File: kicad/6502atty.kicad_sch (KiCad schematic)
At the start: 27 parts, among them J10 Conn_01x04_Pin, J11 Conn_01x03_Pin, J2 Conn_01x02_Pin, J8 Conn_01x03_Pin, U6 27C128, U7 KM62256CLP

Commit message: updates to start v1 rev2, pcb layout updates
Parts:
- added J12: Conn_01x02_Pin, Connector_PinHeader_2.54mm:PinHeader_1x02_P2.54mm_Vertical, symbol Connector:Conn_01x02_Pin
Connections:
- net GND: now also U6.1 (VPP)
- net R~{W}: now also J12.2 (Pin_2)
- net ~{ROM_PGM} renamed ~{ROM_PGM_WE}
- net ~{ROM_PGM_WE}: now also J12.1 (Pin_1)

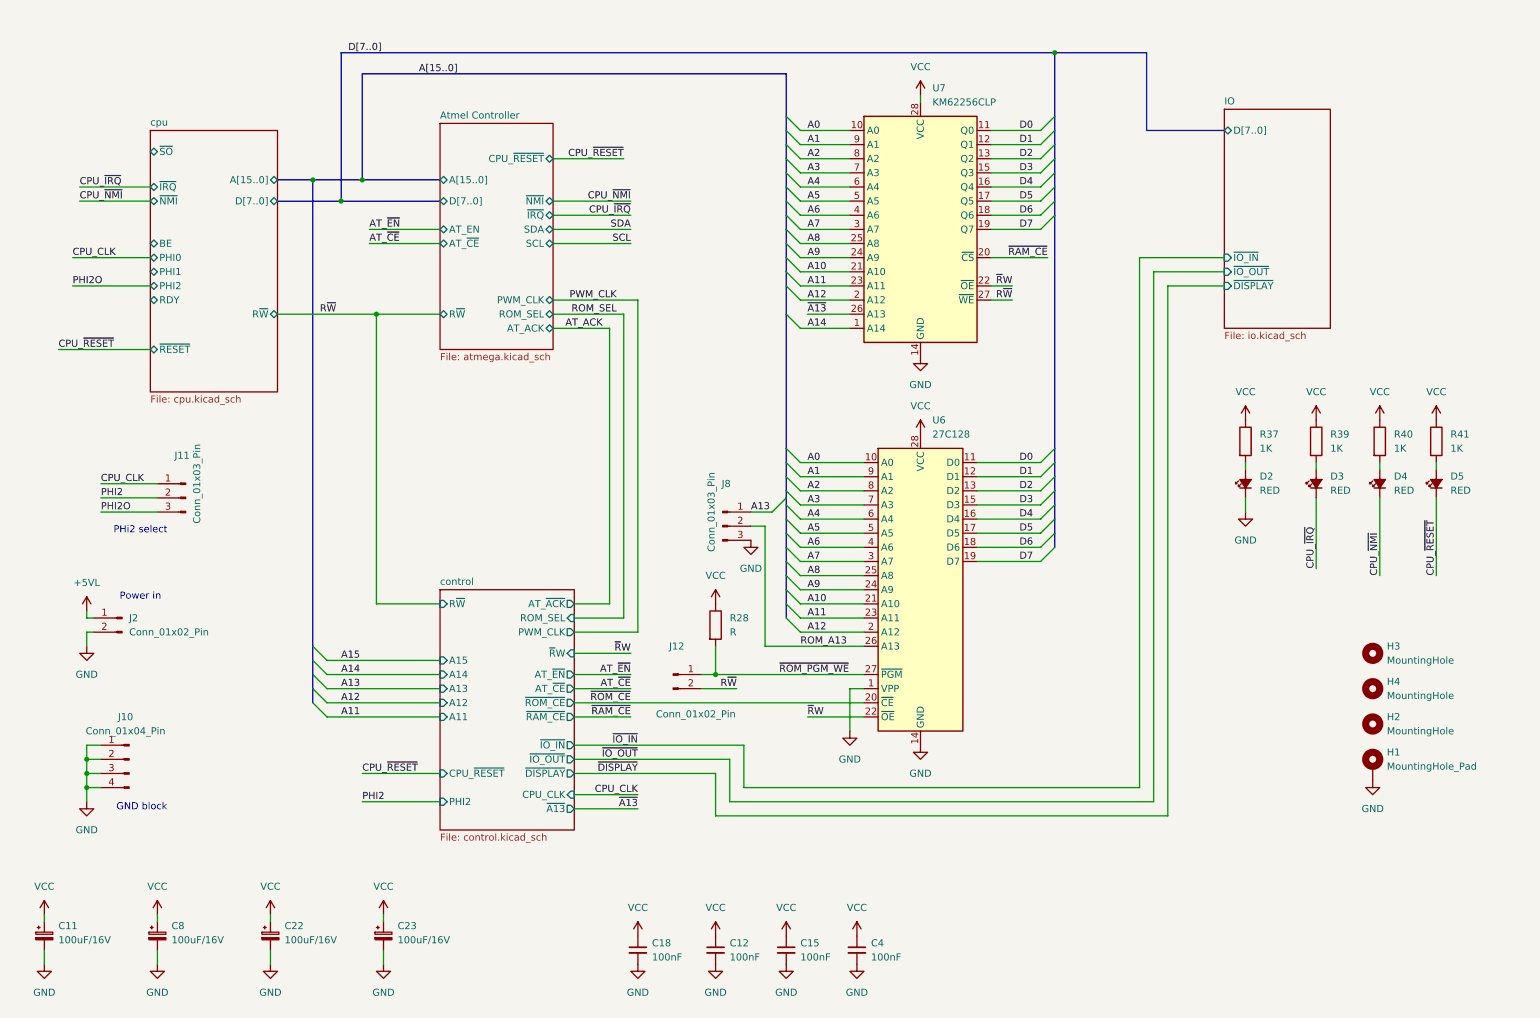
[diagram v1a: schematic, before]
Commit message: value updates, fix ROM ~WE
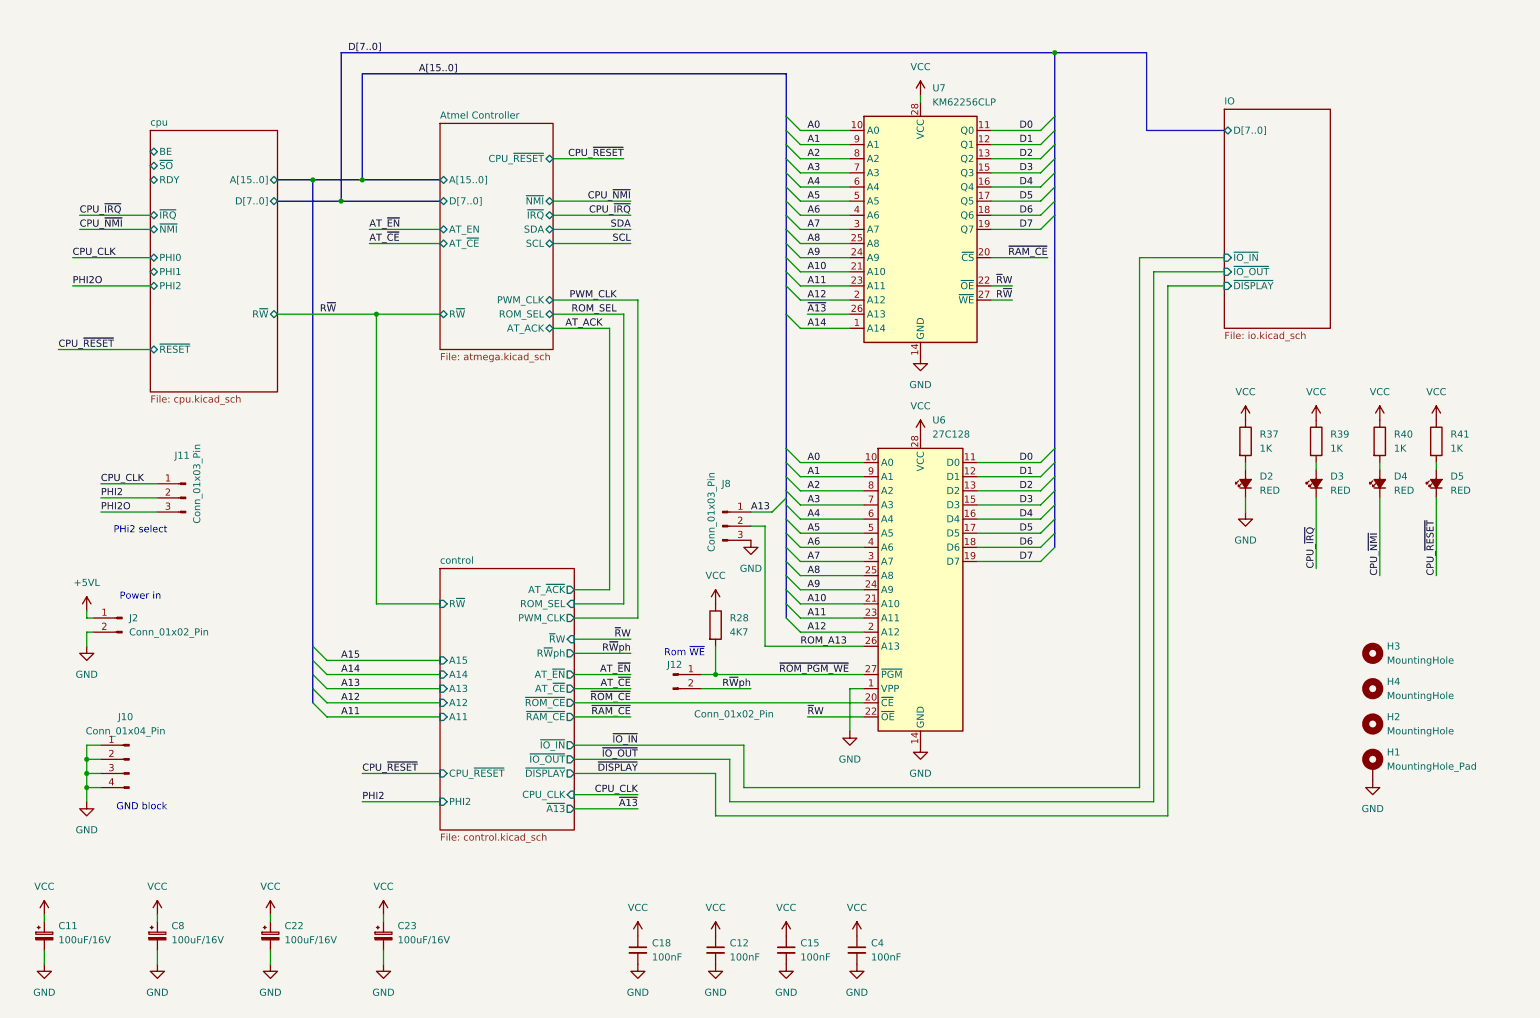
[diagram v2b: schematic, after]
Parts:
- R28: value R -> 4K7
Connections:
- net R~{W}: no longer J12.2 (Pin_2)
- new net R~{W}ph: J12.2 (Pin_2)
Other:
- sheet control ports: added R~{W}ph; removed none
- note added: "Rom ~{WE}"
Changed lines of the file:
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@@
 		)
 	)
+	(text "Rom ~{WE}\n"
+		(exclude_from_sim no)
+		(at 134.112 132.08 0)
+		(effects
+			(font
+				(size 1.27 1.27)
+			)
+		)
+	)
 	(junction
 		(at 200.66 24.13)
@@
 	(wire
 		(pts
-			(xy 114.3 128.27) (xy 125.73 128.27)
+			(xy 114.3 125.73) (xy 125.73 125.73)
 		)
 		(stroke
@@
 	(wire
 		(pts
-			(xy 114.3 123.19) (xy 120.65 123.19)
+			(xy 114.3 120.65) (xy 120.65 120.65)
 		)
 		(stroke
@@
 	(wire
 		(pts
-			(xy 114.3 132.08) (xy 124.46 132.08)
+			(xy 114.3 129.54) (xy 124.46 129.54)
 		)
 		(stroke
@@
 	(wire
 		(pts
-			(xy 123.19 125.73) (xy 114.3 125.73)
+			(xy 123.19 123.19) (xy 114.3 123.19)
 		)
 		(stroke
@@
 	(wire
 		(pts
-			(xy 25.4 50.8) (xy 38.1 50.8)
+			(xy 25.4 55.88) (xy 38.1 55.88)
 		)
 		(stroke
@@
 	(wire
 		(pts
-			(xy 123.19 71.12) (xy 123.19 125.73)
+			(xy 123.19 71.12) (xy 123.19 123.19)
 		)
 		(stroke
@@
 	(wire
 		(pts
-			(xy 120.65 123.19) (xy 120.65 73.66)
+			(xy 120.65 120.65) (xy 120.65 73.66)
 		)
 		(stroke
@@
 	(wire
 		(pts
-			(xy 137.16 138.43) (xy 143.51 138.43)
+			(xy 137.16 138.43) (xy 146.05 138.43)
 		)
 		(stroke
@@
 	(wire
 		(pts
-			(xy 25.4 48.26) (xy 38.1 48.26)
+			(xy 25.4 53.34) (xy 38.1 53.34)
 		)
 		(stroke
@@
 	(wire
 		(pts
-			(xy 125.73 128.27) (xy 125.73 68.58)
+			(xy 125.73 125.73) (xy 125.73 68.58)
 		)
 		(stroke
@@
 	(wire
 		(pts
+			(xy 114.3 132.08) (xy 124.46 132.08)
+		)
+		(stroke
+			(width 0)
+			(type default)
+		)
+	)
+	(wire
+		(pts
 			(xy 220.98 161.29) (xy 220.98 66.04)
 		)
@@
 		)
 	)
+	(label "R~{W}ph"
+		(at 124.46 132.08 180)
+		(effects
+			(font
+				(size 1.27 1.27)
+			)
+			(justify right bottom)
+		)
+	)
 	(label "~{ROM_CE}"
 		(at 124.46 140.97 180)
@@
 	)
 	(label "CPU_~{IRQ}"
-		(at 25.4 48.26 0)
+		(at 25.4 53.34 0)
 		(effects
 			(font
@@
 	)
 	(label "CPU_~{NMI}"
-		(at 25.4 50.8 0)
+		(at 25.4 55.88 0)
 		(effects
 			(font
@@
 		)
 	)
-	(label "R~{W}"
-		(at 143.51 138.43 180)
+	(label "R~{W}ph"
+		(at 146.05 138.43 180)
 		(effects
 			(font
@@
 	)
 	(label "~{R}W"
-		(at 124.46 132.08 180)
+		(at 124.46 129.54 180)
 		(effects
 			(font
@@
 			)
 		)
-		(property "Value" "R"
+		(property "Value" "4K7"
 			(at 142.24 128.2699 0)
 			(effects
@@
 		(dnp no)
 		(property "Reference" "J12"
-			(at 132.715 130.81 0)
+			(at 132.334 134.112 0)
 			(effects
 				(font
@@
 		)
 		(property "Value" "Conn_01x02_Pin"
-			(at 136.144 143.002 0)
+			(at 143.002 143.002 0)
 			(effects
 				(font
@@
 	)
 	(sheet
-		(at 90.17 120.65)
-		(size 24.13 43.18)
+		(at 90.17 116.84)
+		(size 24.13 46.99)
 		(exclude_from_sim no)
 		(in_bom yes)
@@
 		)
 		(property "Sheetname" "control"
-			(at 90.17 119.9384 0)
+			(at 90.17 116.1284 0)
 			(effects
 				(font
@@
 		)
 		(pin "~{R}W" input
-			(at 114.3 132.08 0)
+			(at 114.3 129.54 0)
 			(effects
 				(font
@@
 		)
 		(pin "AT_~{ACK}" output
-			(at 114.3 123.19 0)
+			(at 114.3 120.65 0)
 			(effects
 				(font
@@
 		)
 		(pin "ROM_SEL" input
-			(at 114.3 125.73 0)
+			(at 114.3 123.19 0)
 			(effects
 				(font
@@
 		)
 		(pin "PWM_CLK" output
-			(at 114.3 128.27 0)
+			(at 114.3 125.73 0)
 			(effects
 				(font
@@
 			)
 		)
+		(pin "R~{W}ph" output
+			(at 114.3 132.08 0)
+			(effects
+				(font
+					(size 1.27 1.27)
+				)
+				(justify right)
+			)
+		)
 		(instances
 			(project "6502atty"
@@
 		)
 		(pin "BE" bidirectional
-			(at 38.1 58.42 180)
+			(at 38.1 41.91 180)
 			(effects
 				(font
@@
 		)
 		(pin "RDY" bidirectional
-			(at 38.1 68.58 180)
+			(at 38.1 46.99 180)
 			(effects
 				(font
@@
 		)
 		(pin "~{IRQ}" bidirectional
-			(at 38.1 48.26 180)
+			(at 38.1 53.34 180)
 			(effects
 				(font
@@
 		)
 		(pin "~{NMI}" bidirectional
-			(at 38.1 50.8 180)
+			(at 38.1 55.88 180)
 			(effects
 				(font
@@
 		)
 		(pin "~{SO}" bidirectional
-			(at 38.1 41.91 180)
+			(at 38.1 44.45 180)
 			(effects
 				(font

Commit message: more updates for v1 rev2
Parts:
- R39, R40: footprint Resistor_THT:R_Axial_DIN0207_L6.3mm_D2.5mm_P2.54mm_Vertical -> Resistor_THT:R_Axial_DIN0207_L6.3mm_D2.5mm_P10.16mm_Horizontal
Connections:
- net A15: now also U7.20 (~{CS})
- net R~{W}: no longer U7.27 (~{WE})
- net R~{W}ph: now also U7.27 (~{WE})
- net ~{RAM_CE}: no longer U7.20 (~{CS})
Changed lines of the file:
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@@
 	(wire
 		(pts
-			(xy 189.23 68.58) (xy 193.04 68.58)
+			(xy 189.23 68.58) (xy 195.58 68.58)
 		)
 		(stroke
@@
 	(wire
 		(pts
-			(xy 189.23 60.96) (xy 199.39 60.96)
+			(xy 189.23 60.96) (xy 195.58 60.96)
 		)
 		(stroke
@@
 	(wire
 		(pts
-			(xy 189.23 66.04) (xy 193.04 66.04)
+			(xy 189.23 66.04) (xy 195.58 66.04)
 		)
 		(stroke
@@
 		)
 	)
-	(label "~{RAM_CE}"
-		(at 199.39 60.96 180)
-		(effects
-			(font
-				(size 1.27 1.27)
-			)
-			(justify right bottom)
-		)
-	)
 	(label "D5"
 		(at 194.31 110.49 0)
@@
 		)
 	)
+	(label "A15"
+		(at 195.58 60.96 180)
+		(effects
+			(font
+				(size 1.27 1.27)
+			)
+			(justify right bottom)
+		)
+	)
 	(label "AT_~{EN}"
 		(at 124.46 135.89 180)
@@
 	)
 	(label "~{R}W"
-		(at 193.04 66.04 180)
+		(at 195.58 66.04 180)
 		(effects
 			(font
@@
 		)
 	)
+	(label "R~{W}ph"
+		(at 195.58 68.58 180)
+		(effects
+			(font
+				(size 1.27 1.27)
+			)
+			(justify right bottom)
+		)
+	)
 	(label "SCL"
 		(at 124.46 58.42 180)
@@
 		)
 	)
-	(label "R~{W}"
-		(at 193.04 68.58 180)
-		(effects
-			(font
-				(size 1.27 1.27)
-			)
-			(justify right bottom)
-		)
-	)
 	(label "A4"
 		(at 156.21 107.95 0)
@@
 			)
 		)
-		(property "Footprint" "Resistor_THT:R_Axial_DIN0207_L6.3mm_D2.5mm_P2.54mm_Vertical"
+		(property "Footprint" "Resistor_THT:R_Axial_DIN0207_L6.3mm_D2.5mm_P10.16mm_Horizontal"
 			(at 257.302 93.98 90)
 			(effects
@@
 			)
 		)
-		(property "Footprint" "Resistor_THT:R_Axial_DIN0207_L6.3mm_D2.5mm_P2.54mm_Vertical"
+		(property "Footprint" "Resistor_THT:R_Axial_DIN0207_L6.3mm_D2.5mm_P10.16mm_Horizontal"
 			(at 245.872 93.98 90)
 			(effects

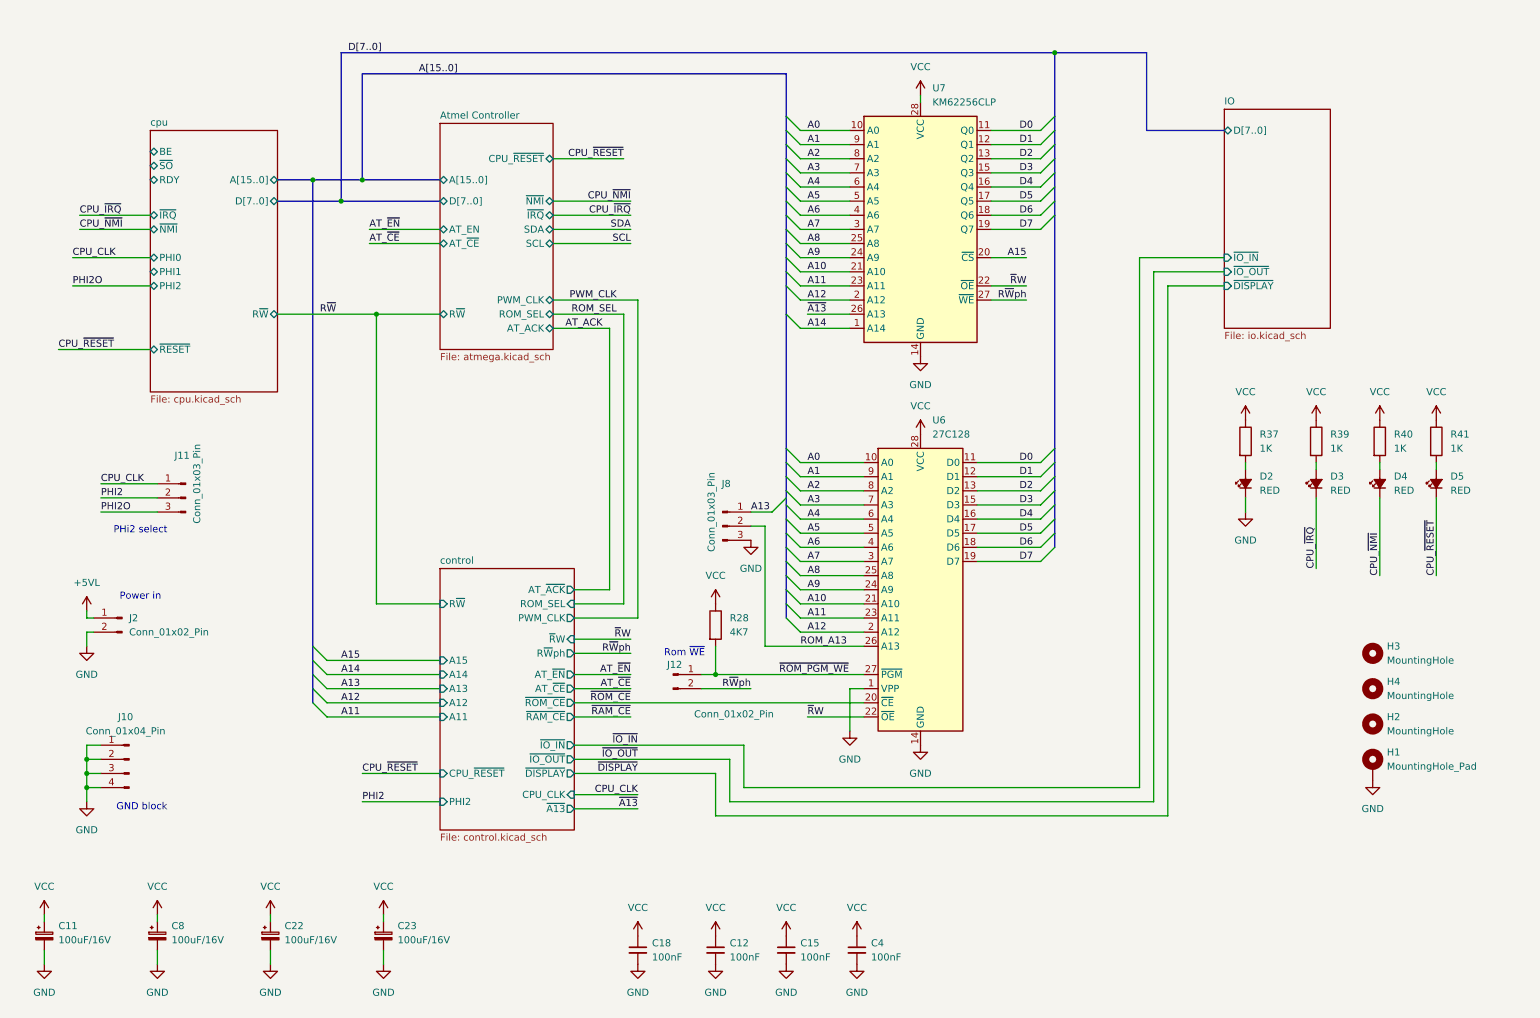
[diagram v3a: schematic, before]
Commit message: pcb: add option for radial instead of axial capacitors
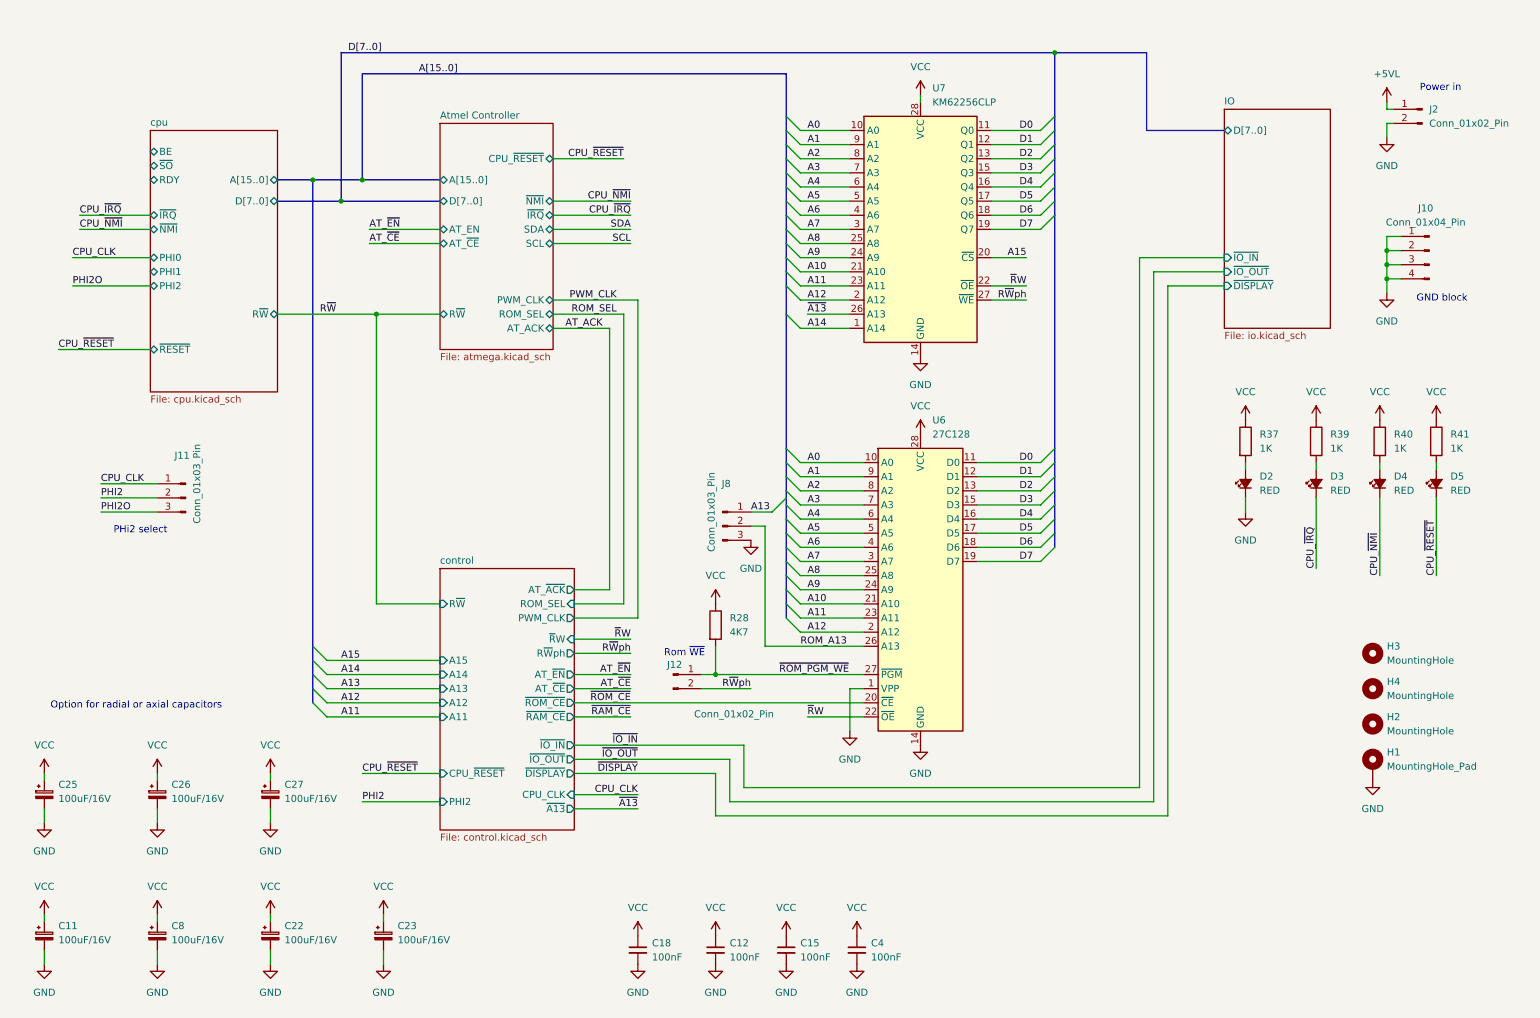
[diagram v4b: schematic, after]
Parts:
- added C25, C26, C27: 100uF/16V, Capacitor_THT:CP_Radial_D6.3mm_P2.50mm, symbol Device:C_Polarized_Small
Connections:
- net GND: now also C25.2, C26.2, C27.2
- net VCC: now also C25.1, C26.1, C27.1
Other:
- note added: "Option for radial or axial capacitors"
- moved on the sheet: J10, J2

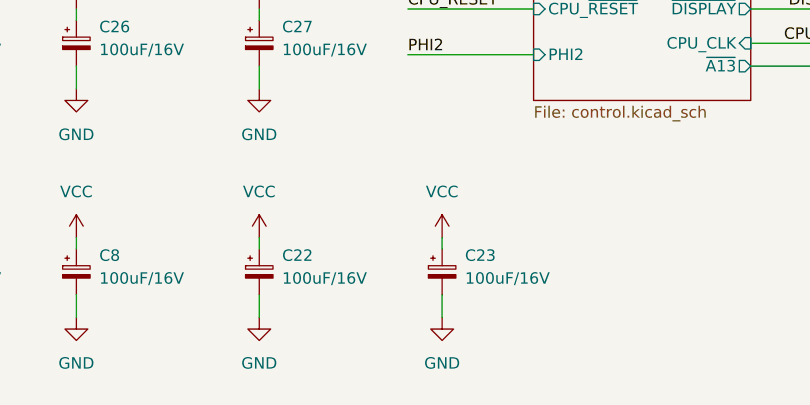
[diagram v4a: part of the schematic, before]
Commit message: pcb: route tidying, reduce size, re-do teardrops
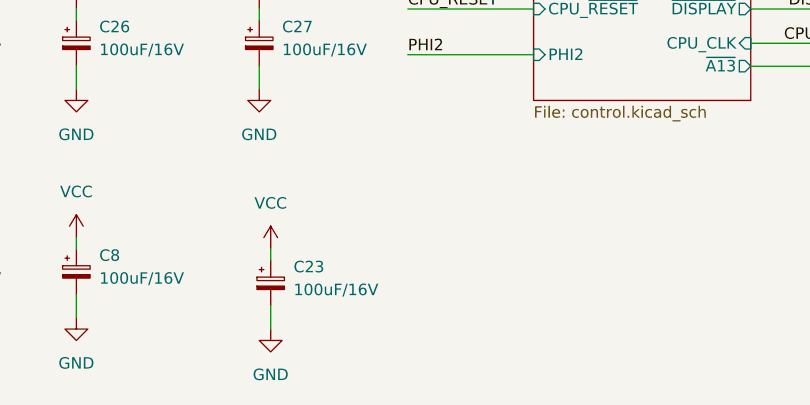
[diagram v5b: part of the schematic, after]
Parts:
- removed C22: 100uF/16V, Capacitor_THT:CP_Axial_L10.0mm_D6.0mm_P15.00mm_Horizontal, symbol Device:C_Polarized_Small
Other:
- moved on the sheet: C23
